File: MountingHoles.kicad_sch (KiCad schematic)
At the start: 12 parts

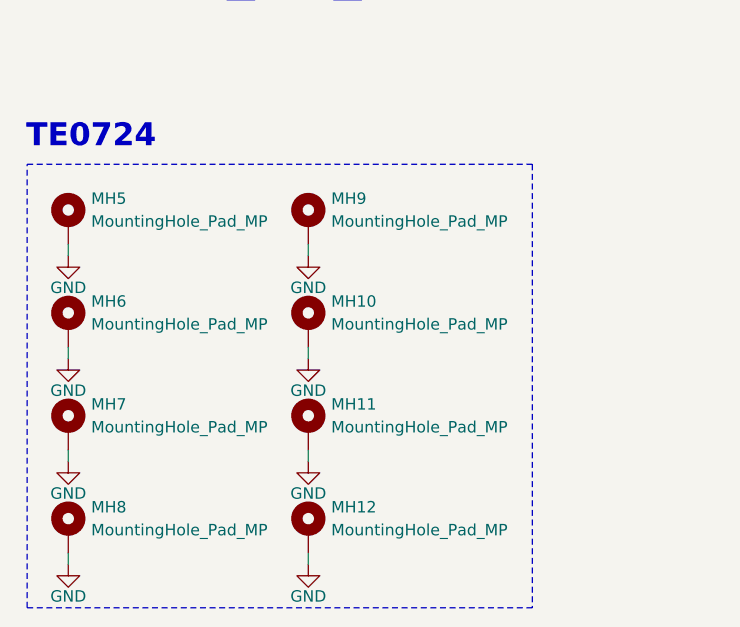
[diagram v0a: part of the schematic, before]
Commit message: Moved SD Card Slot
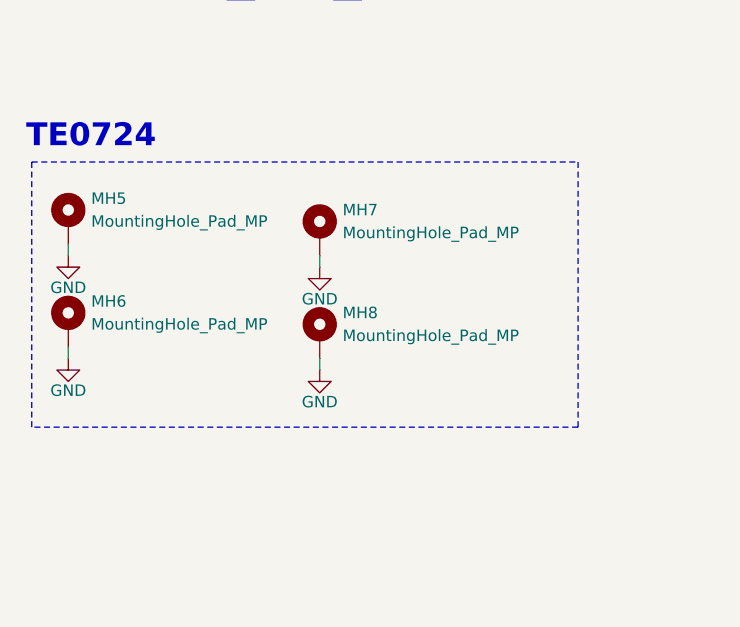
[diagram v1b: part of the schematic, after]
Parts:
- removed MH10, MH11, MH12, MH9: MountingHole_Pad_MP, MountingHole:MountingHole_2.2mm_M2_Pad_Via, symbol Mechanical:MountingHole_Pad_MP
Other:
- moved on the sheet: MH7, MH8

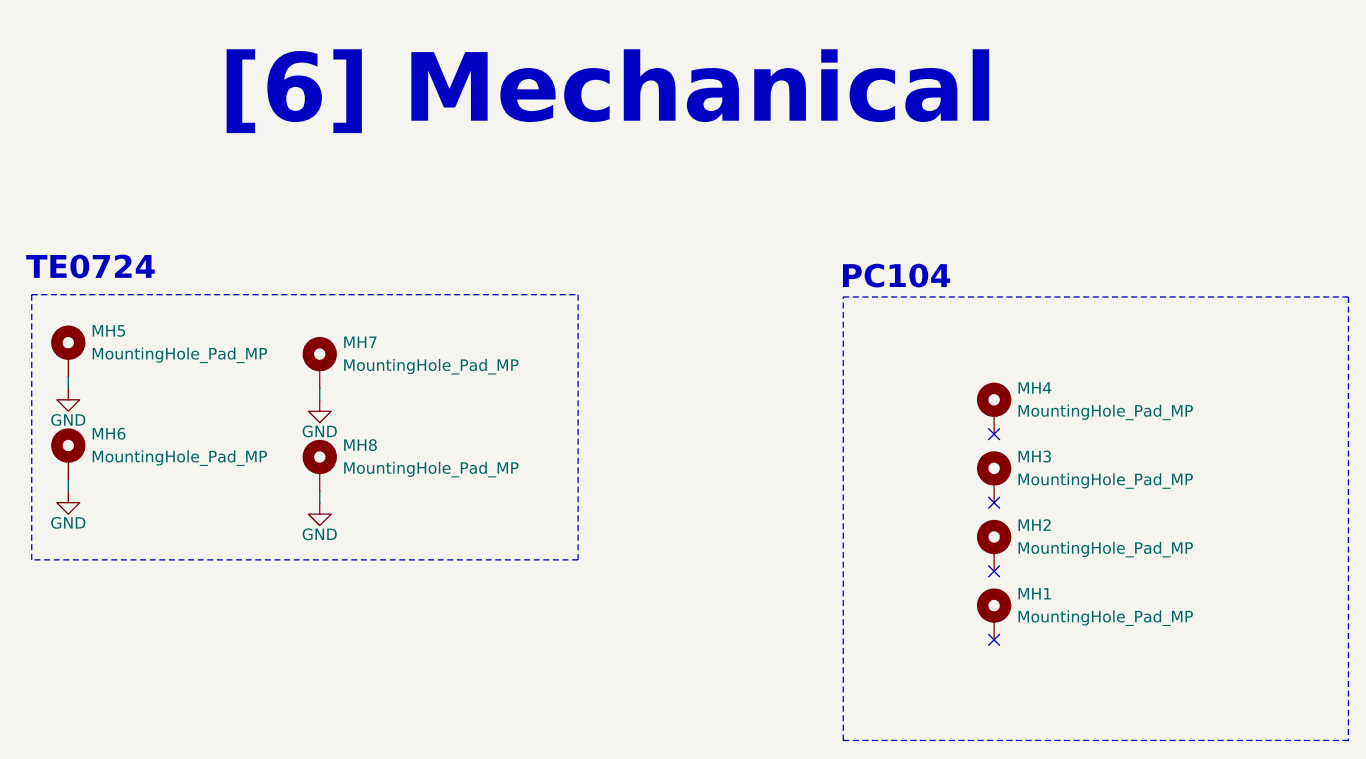
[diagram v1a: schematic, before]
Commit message: Added level shifter and breakout for ethernet
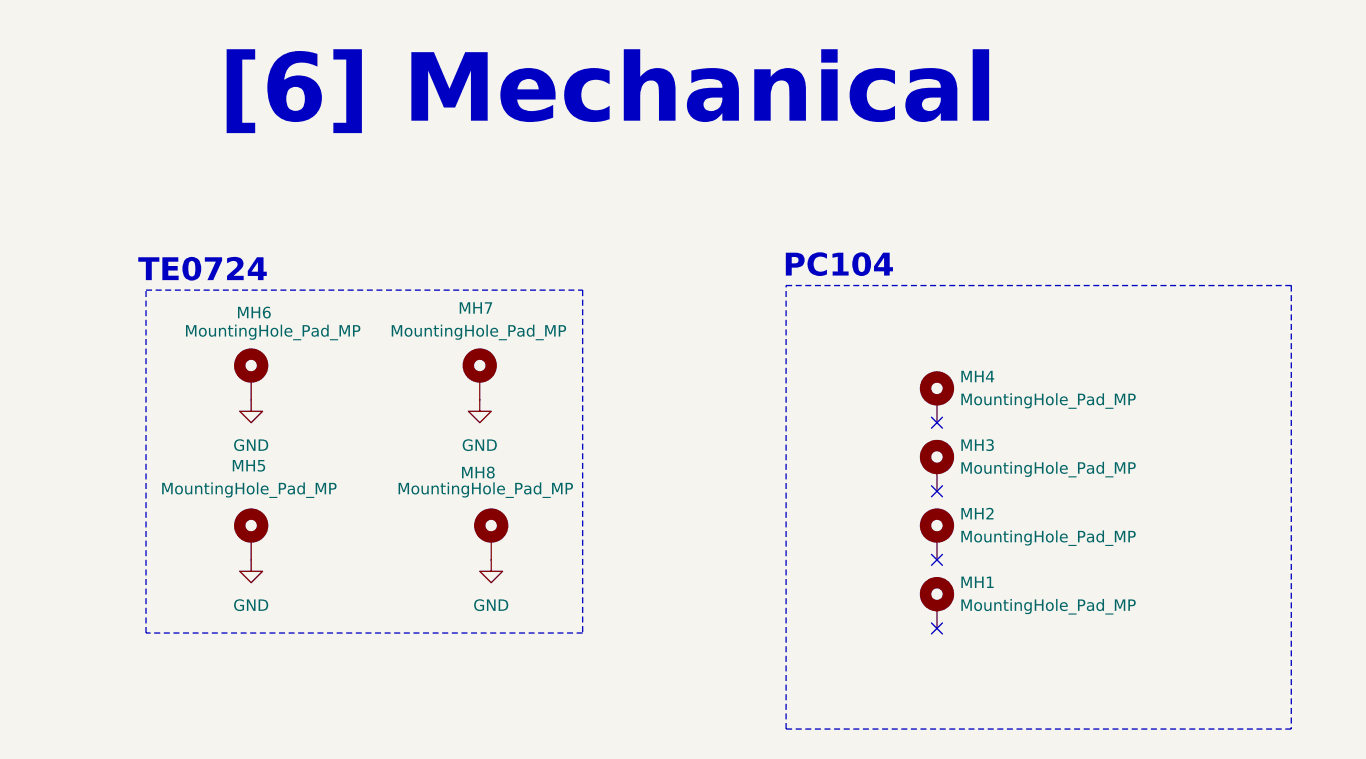
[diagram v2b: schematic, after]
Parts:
- MH5, MH6, MH7, MH8: footprint MountingHole:MountingHole_2.2mm_M2_Pad_Via -> MountingHole:MountingHole_2.2mm_M2_Pad
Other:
- moved on the sheet: MH1, MH2, MH3, MH4, MH5, MH6, MH7, MH8
